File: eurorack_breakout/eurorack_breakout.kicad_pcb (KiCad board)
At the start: 2 copper layers, 50.8 x 34.9 mm, 14 parts, among them J1 Conn_02x08_Odd_Even, J2 Conn_01x08_Male, U1 LM1117-3.3, U2 LM1117-5.0

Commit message: eh, different license
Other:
- board text added: "16-Pin Eurorack Power Breakout Optional Regulated +3V3, +3V3A, +5V (c) 2021 Zachary Hart CC BY-SA-4.0 rev0.1"
- board text removed: "16-Pin Eurorack Power Breakout Optional Regulated +3V3, +3V3A, +5V (c) 2021 Zachary Hart CC BY-NC-SA"

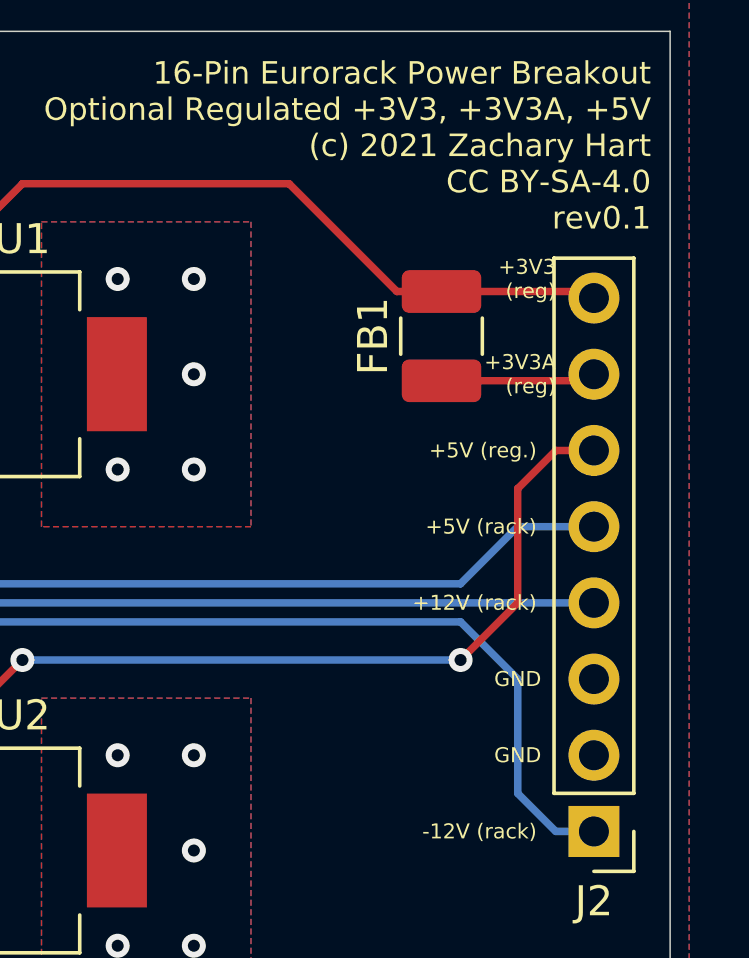
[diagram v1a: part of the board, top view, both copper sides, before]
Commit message: test points for 3V3 and 5V on pcb
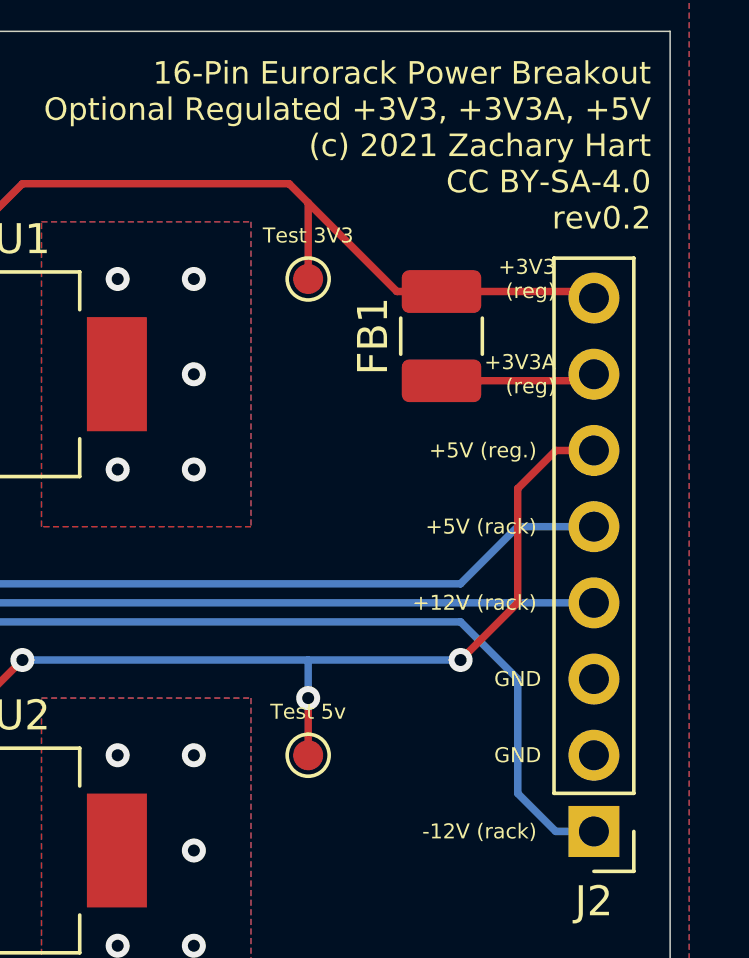
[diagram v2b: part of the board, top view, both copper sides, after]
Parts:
- added Test 3V3: TestPoint_Pad_D1.0mm, TestPoint:TestPoint_Pad_D1.0mm, F.Cu at (148.0, 87.0)
- added Test 5v: TestPoint_Pad_D1.0mm, TestPoint:TestPoint_Pad_D1.0mm, F.Cu at (148.0, 102.9)
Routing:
- net BOARD_5V: track 47.5 -> 50.7 mm, vias 10 -> 11
- net BOARD_3V3: track 51.0 -> 53.6 mm
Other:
- board text added: "16-Pin Eurorack Power Breakout Optional Regulated +3V3, +3V3A, +5V (c) 2021 Zachary Hart CC BY-SA-4.0 rev0.2"
- board text removed: "16-Pin Eurorack Power Breakout Optional Regulated +3V3, +3V3A, +5V (c) 2021 Zachary Hart CC BY-SA-4.0 rev0.1"

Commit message: board rev0.2
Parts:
- moved 5V 7.62 mm to (119.4, 100.3)
- moved C2 7.62 mm to (127.0, 100.3)
- moved C3 7.62 mm to (127.0, 92.7)
- moved C6 0.64 mm to (135.3, 98.4)
- moved Test 5v 0.64 mm to (148.0, 102.2)
- moved U2 0.64 mm to (138.4, 105.4)
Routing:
- net BOARD_3V3: track 53.6 -> 47.8 mm, vias 9 -> 26
- net RACK_12V: track 106.8 -> 104.7 mm
- net BOARD_5V: track 50.7 -> 51.5 mm, vias 11 -> 29
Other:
- board size 50.8 x 34.9 mm -> 50.8 x 34.3 mm
- net class Eurorack 12V added: clearance 0.3, trace_width 0.4, via_dia 0.8, via_drill 0.5
- board text added: "16-Pin Eurorack Power Breakout (c) 2021 Zachary Hart CC BY-SA-4.0 rev0.2"
- board text removed: "16-Pin Eurorack Power Breakout Optional Regulated +3V3, +3V3A, +5V (c) 2021 Zachary Hart CC BY-SA-4.0 rev0.2"

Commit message: goodbye miku :(
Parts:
- removed G***: LOGO, zzzzzzzz:small_miku
- added Ref**: Val**, zzzzzzzz:zzzzzzzz_back_no_cu, F.Cu at (151.8, 108.6)

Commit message: flip breadboard-side silkscreen around
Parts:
- J2: moved to B.Cu
- turned J2 to 0 degrees
